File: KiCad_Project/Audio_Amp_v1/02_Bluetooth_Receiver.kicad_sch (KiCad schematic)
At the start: 0 parts

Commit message: Updated Power management section, Bluetooth receiver and connectors. Added some components footprints and 3D.
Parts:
- added C30: 1u, symbol Device:C
- added C31: 100n, symbol Device:C
- added D1: LED, symbol Device:LED
- added IC3: BM64SPKS1MC2-0002AA, BM64SPKS1MC20002AA, symbol BM64SPKS1MC2-0002AA:BM64SPKS1MC2-0002AA
- added Q1: NMOS, symbol Simulation_SPICE:NMOS
- added R10, R11, R12, R13, R14: 10k, symbol Device:R_US
- added R15: 100k, symbol Device:R_US
- added R16: 330, symbol Device:R_US
- added TP1, TP2: TestPoint, TestPoint:TestPoint_Pad_D2.0mm, symbol Connector:TestPoint
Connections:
- new net: Q1.2 (G), R14.2, R15.2
- new net: D1.2 (A), R16.1
- new net: IC3.41 (P2_0), R13.2
- new net: IC3.26 (MFB), R11.1
- new net: D1.1 (K), IC3.28 (LED1)
- new net: IC3.32 (EAN), R12.2
- new net +3.3V: C30.1, C31.1, IC3.22 (BAT_IN), R10.1, R13.1
- new net BT_COM: IC3.6 (AOHPM)
- new net BT_OUT_L: IC3.7 (AOHPL)
- new net BT_OUT_R: IC3.5 (AOHPR)
- new net GNDA: C30.2, C31.2, IC3.14 (GND_1), IC3.43 (GND_2), Q1.3 (S), R12.1, R15.1
- new net RST_N: IC3.13 (RST_N), Q1.1 (D), R10.2, TP2.1
- new net SYS_PWR: IC3.24 (SYS_PWR), R11.2, R16.2, TP1.1
- new net UART_RX: IC3.19 (HCI_RXD)
- new net UART_TX: IC3.20 (HCI_TXD)
- new net USB_5V: R14.1
- no-connect marks 0 -> 29
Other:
- note added: "Flash Application*"
- note added: "When USB-C is connected, the Bluetooth Module goes OFF"

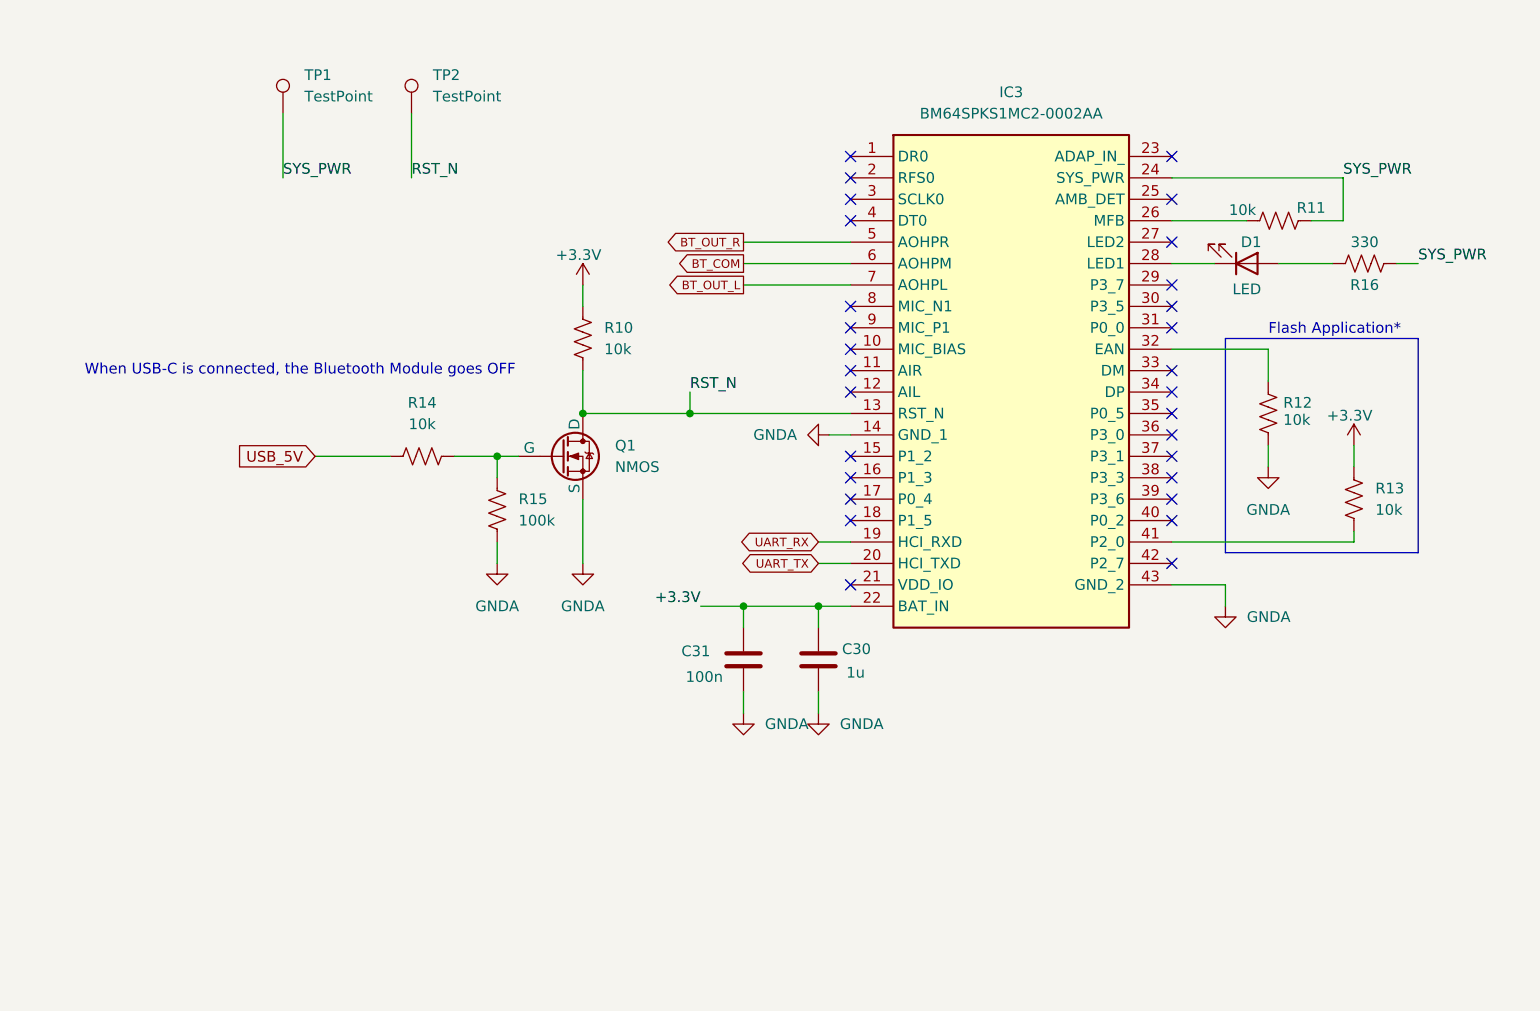
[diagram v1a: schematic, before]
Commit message: Remove KiCad .history from tracking, add to gitignore
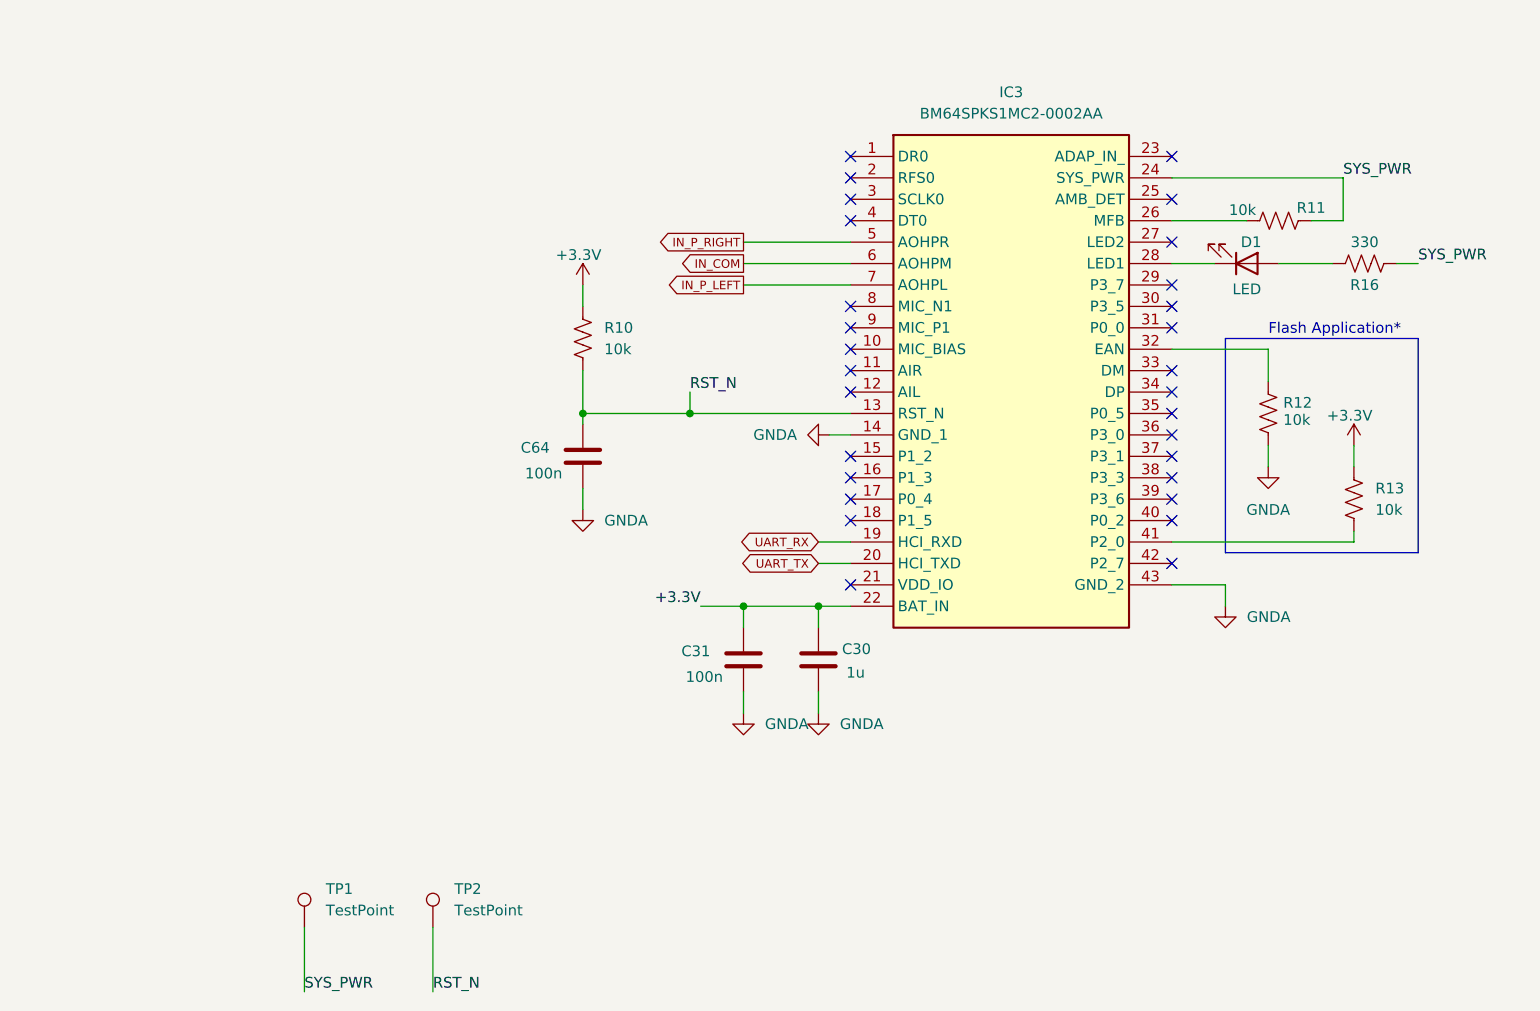
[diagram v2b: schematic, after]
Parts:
- removed Q1: NMOS, symbol Simulation_SPICE:NMOS
- removed R14: 10k, symbol Device:R_US
- removed R15: 100k, symbol Device:R_US
- added C64: 100n, symbol Device:C
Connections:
- net GNDA: now also C64.2
- net RST_N: now also C64.1
- net BT_COM renamed IN_COM
- net BT_OUT_L renamed IN_P_LEFT
- net BT_OUT_R renamed IN_P_RIGHT
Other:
- note removed: "When USB-C is connected, the Bluetooth Module goes OFF"
- moved on the sheet: TP1, TP2

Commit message: Finished Schematic and started Layout
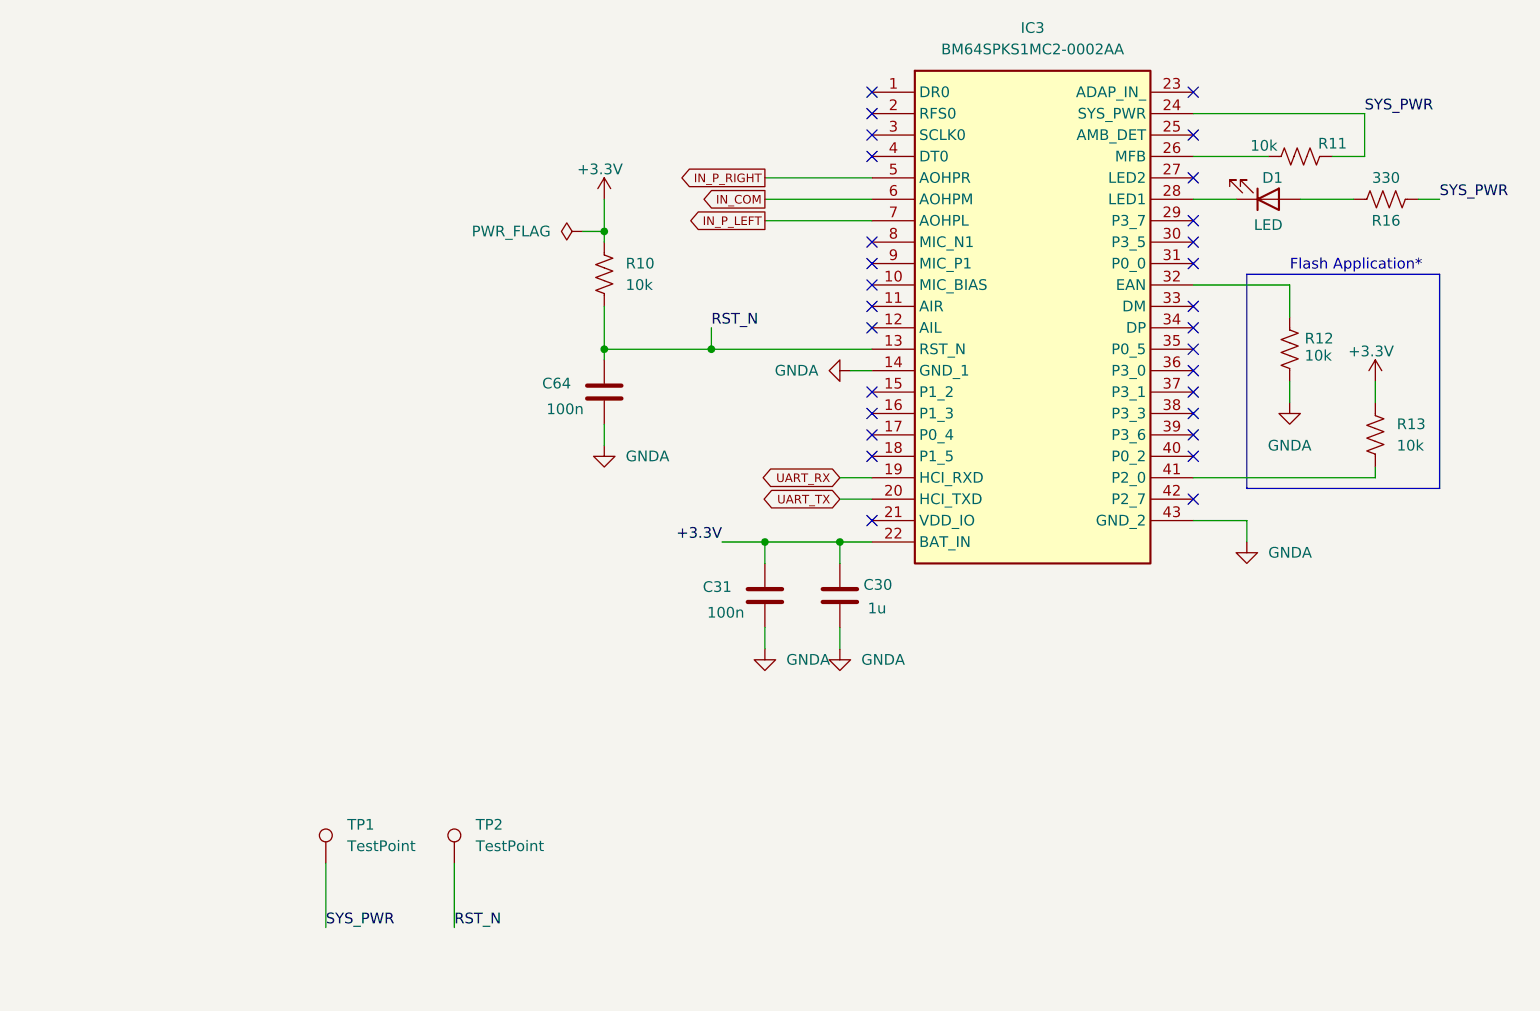
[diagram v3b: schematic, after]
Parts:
- C30, C31, C64: footprint (none) -> Capacitor_SMD:C_0603_1608Metric
- D1: footprint (none) -> Diode_SMD:D_0805_2012Metric
- R10, R11, R12, R13, R16: footprint (none) -> Resistor_SMD:R_0603_1608Metric
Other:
- moved on the sheet: C30, C31, C64, D1, IC3, R10, R11, R12, R13, R16, TP1, TP2
